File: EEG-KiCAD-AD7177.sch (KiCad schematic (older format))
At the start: 54 parts, among them J1 Conn_01x06, J2 Conn_01x02, J3 Conn_01x02, J4 Conn_01x05, U1 AD7177-2, U2 OPAMP, U3 NRF528XX-QFAA, U4 RP511Z331_3.3V, U5 XCL101A501-5V, X1 Crystal_GND24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

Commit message: Done
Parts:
- removed C13: N.C., symbol EEG-KiCAD-AD7177-rescue:C-EEG_ADS1299-rescue
- A1: footprint (none) -> RF_Antenna:JTI-2450AT18A100-CHIP-ANT
- C1, C10, C2, C23, C25, C26, C27, C3, C4, C5, C6, C7, C8, C9: footprint (none) -> Capacitor_SMD:C_0402_1005Metric
- C11, C22: footprint Capacitors_SMD:C_0603 -> Capacitor_SMD:C_0402_1005Metric
- C12, C14, C15, C16, C17, C18, C19, C20, C21: footprint Capacitors_SMD:C_0402 -> Capacitor_SMD:C_0402_1005Metric
- F1: footprint (none) -> Capacitor_SMD:Modified_cap-0402-ground
- J1: value Conn_01x06 -> IN EEG; footprint (none) -> Connector_PinHeader_2.54mm:PinHeader_1x06_P2.54mm_Vertical
- J2: value Conn_01x02 -> Battery; footprint (none) -> Connector_PinHeader_2.54mm:PinHeader_1x02_P2.54mm_Vertical
- J3: value Conn_01x02 -> Programmer; footprint (none) -> Connector_PinHeader_2.54mm:PinHeader_1x02_P2.54mm_Vertical
- J4: value Conn_01x05 -> Vs+ Ele; footprint (none) -> Connector_PinHeader_2.54mm:PinHeader_1x05_P2.54mm_Vertical
- J5: renamed from J?; value Conn_01x05 -> Vs- Ele; footprint (none) -> Connector_PinHeader_2.54mm:PinHeader_1x05_P2.54mm_Vertical
- L1: footprint Inductors_SMD:L_0603 -> Inductor_SMD:L_0603_1608Metric
- L2, L3, L4: footprint Inductors_SMD:L_0402 -> Inductor_SMD:L_0402_1005Metric
- L5: footprint (none) -> Inductor_SMD:L_0603_1608Metric
- R1, R2, R3, R4, R5, R6, R7: footprint (none) -> Resistor_SMD:R_0402_1005Metric
- R8: footprint (none) -> Resistor_SMD:R_0603_1608Metric
- U1: footprint (none) -> SOP65P640X120-24N:SOP65P640X120-24N; symbol Project_Lib:AD7177-2 -> EEG-KiCAD-AD7177-rescue:AD7177-2-Project_Lib
- U2: value OPAMP -> OPA2210; footprint (none) -> Package_SO:VSSOP-8_3.0x3.0mm_P0.65mm
- U4: footprint (none) -> Package_LGA:RP511Z331
- U5: footprint (none) -> CONV_XCL206B333CR-G:CONV_XCL206B333CR-G; symbol Project_Lib:XCL101A501 -> EEG-KiCAD-AD7177-rescue:XCL101A501-Project_Lib
- X2: footprint Crystals:Crystal_SMD_2012-2pin_2.0x1.2mm -> Crystal:Crystal_SMD_2012-2Pin_2.0x1.2mm
- X3: renamed from 16MHz1; footprint (none) -> Crystal:Crystal_SMD_2520-4Pin_2.5x2.0mm
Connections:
- net labels removed: DEC2
- wire segments 251 -> 249
- no-connect marks 27 -> 28

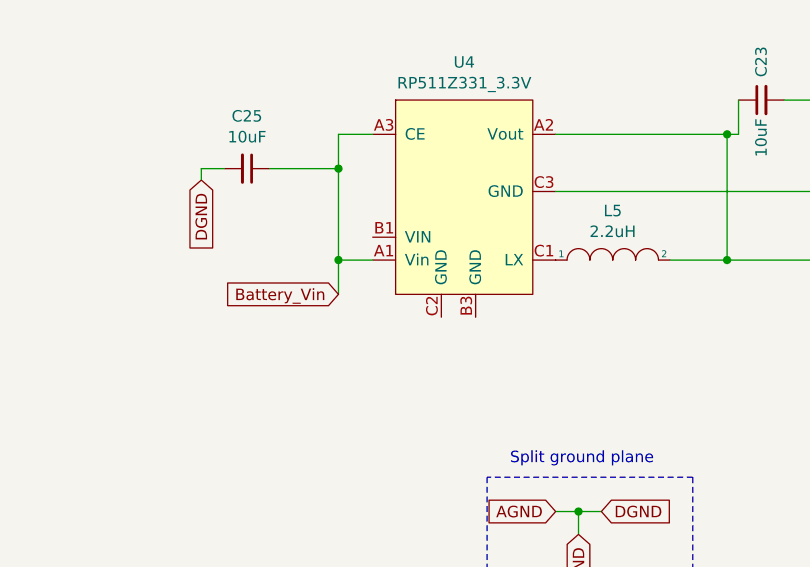
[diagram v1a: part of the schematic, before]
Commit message: Fixed pins
Fixed wrong pins
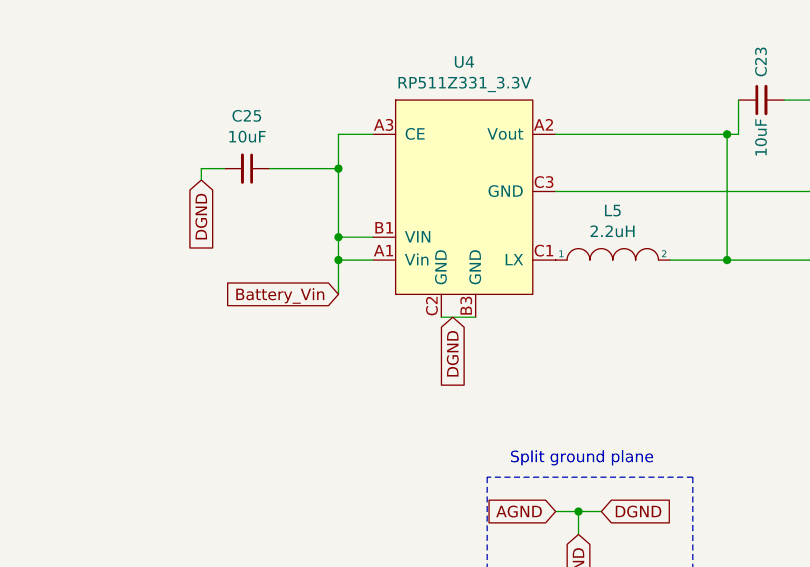
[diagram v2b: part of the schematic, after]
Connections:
- net +4V: now also U4.B1 (VIN)
- net AGND: now also U4.B3 (GND), U4.C2 (GND)
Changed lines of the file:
@@
 Connection ~ 12500 4600
 Wire Wire Line
-	12500 4600 12500 5000
+	12500 4600 12500 4900
 $Comp
 L Device:C_Small C25
@@
 NoConn ~ 4300 9250
 NoConn ~ 4400 9250
+Wire Wire Line
+	12650 4900 12500 4900
+Connection ~ 12500 4900
+Wire Wire Line
+	12500 4900 12500 5000
+Wire Wire Line
+	13100 5250 12950 5250
+Text GLabel 13000 5250 3    50   Input ~ 0
+DGND
 $EndSCHEMATC
